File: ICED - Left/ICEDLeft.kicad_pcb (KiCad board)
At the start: 2 copper layers, 175.4 x 145 mm, 148 parts, among them P1 FLASH_HDR, P2 USBC, P3 CONN_17, P4 USB3_AFEMALE, Q1 TC1264, U1 MK20DX256VLH7, X1 CRYSTAL

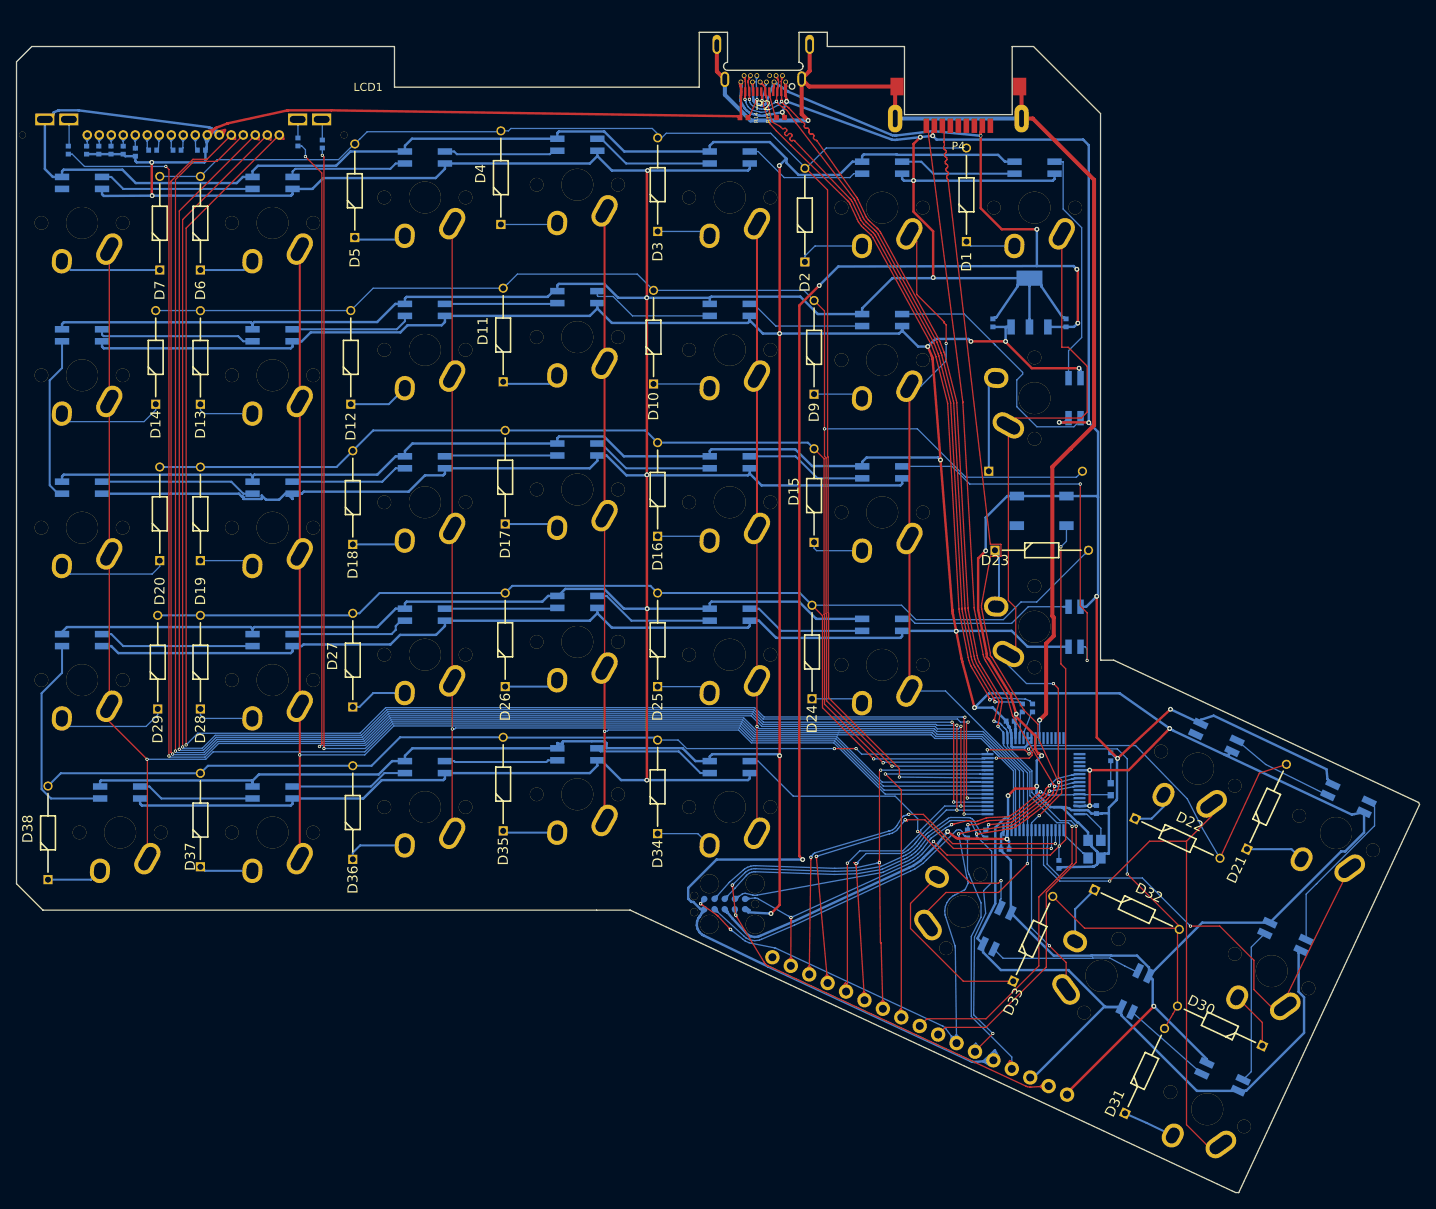
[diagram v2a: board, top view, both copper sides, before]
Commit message: RGB headers and finishing touches!
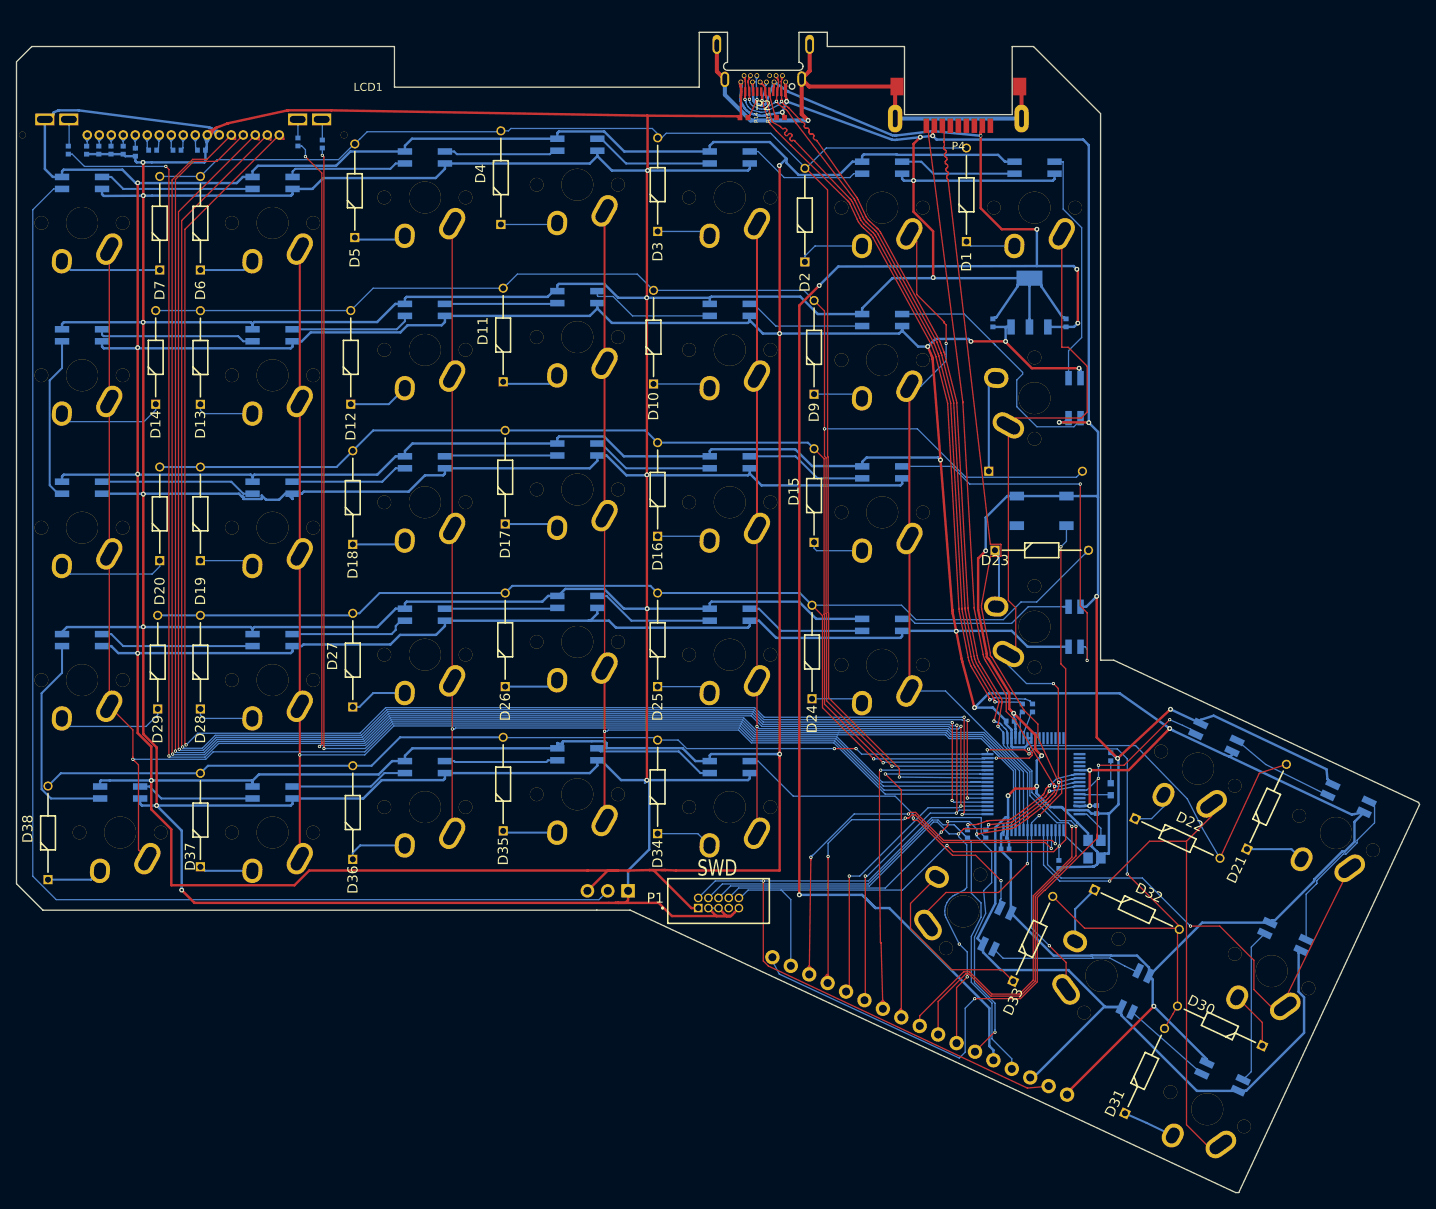
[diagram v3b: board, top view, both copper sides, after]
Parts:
- added P5: RGB Out, Connector_PinHeader_2.54mm:PinHeader_1x03_P2.54mm_Horizontal, B.Cu at (94.1, 133.1)
- P1: value FLASH_HDR -> Conn_ARM_JTAG_SWD_10; footprint prettylib:JLINK_NEEDLE -> prettylib:SHF-105-01-L-D-TH; moved to F.Cu
- moved P1 0.77 mm to (105.4, 134.6), turned to 0 degrees
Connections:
- LED22 pad 4: (no net) -> /ledmatrix/RGBIN
- LED7 pad 2: (no net) -> /ledmatrix/RGBOUT
- P1 pad 5: +5V -> VSS
- P1 pad 7: /mcu/TX2 -> (no net)
- P1 pad 9: /mcu/PTA5 -> VSS
- P3 pad 17: (no net) -> /ledmatrix/RGBIN
- U1 pad 10: /GND -> (no net)
- U1 pad 26: (no net) -> /ledmatrix/RGBIN
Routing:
- net VDD: track 974.2 -> 1142.2 mm, vias 15 -> 19
- net /ledmatrix/RGBOUT: track 0.00 -> 162.0 mm
- net VSS: track 1170.4 -> 1320.3 mm, vias 25 -> 28
- net /ledmatrix/RGBIN: track 0.00 -> 92.8 mm, vias 0 -> 4
- net /GND: track 149.8 -> 64.7 mm, vias 2 -> 1
- net /mcu/PTA5: track 54.0 -> 3.91 mm, vias 2 -> 0
- net +5V: track 248.6 -> 222.8 mm
- net /mcu/TX2: track 70.2 -> 45.2 mm, vias 2 -> 1
- net /mcu/TX0: track 177.4 -> 169.7 mm
- net /mcu/RX1: track 155.3 -> 160.3 mm
- net /mcu/SCLK: track 232.7 -> 227.8 mm
- net /mcu/TX1: track 158.4 -> 162.0 mm
- net /mcu/MOSI: track 232.5 -> 229.6 mm
- net /mcu/RX0: track 177.1 -> 174.4 mm, vias 3 -> 5
- net /Col9: track 189.3 -> 191.1 mm
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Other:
- board text added: "Based on Ergodox Infinity v1.2b"
- board text added: "Ergodox Aleph 1 by @stillinbeta"
- board text added: "RGB Out"
- board text added: "RGBIN"
- board text added: "SWD"
- board text removed: "AUD"
- board text removed: "Ergodox Aleph v0.1 by @stillinbeta"

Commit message: Footprints placed
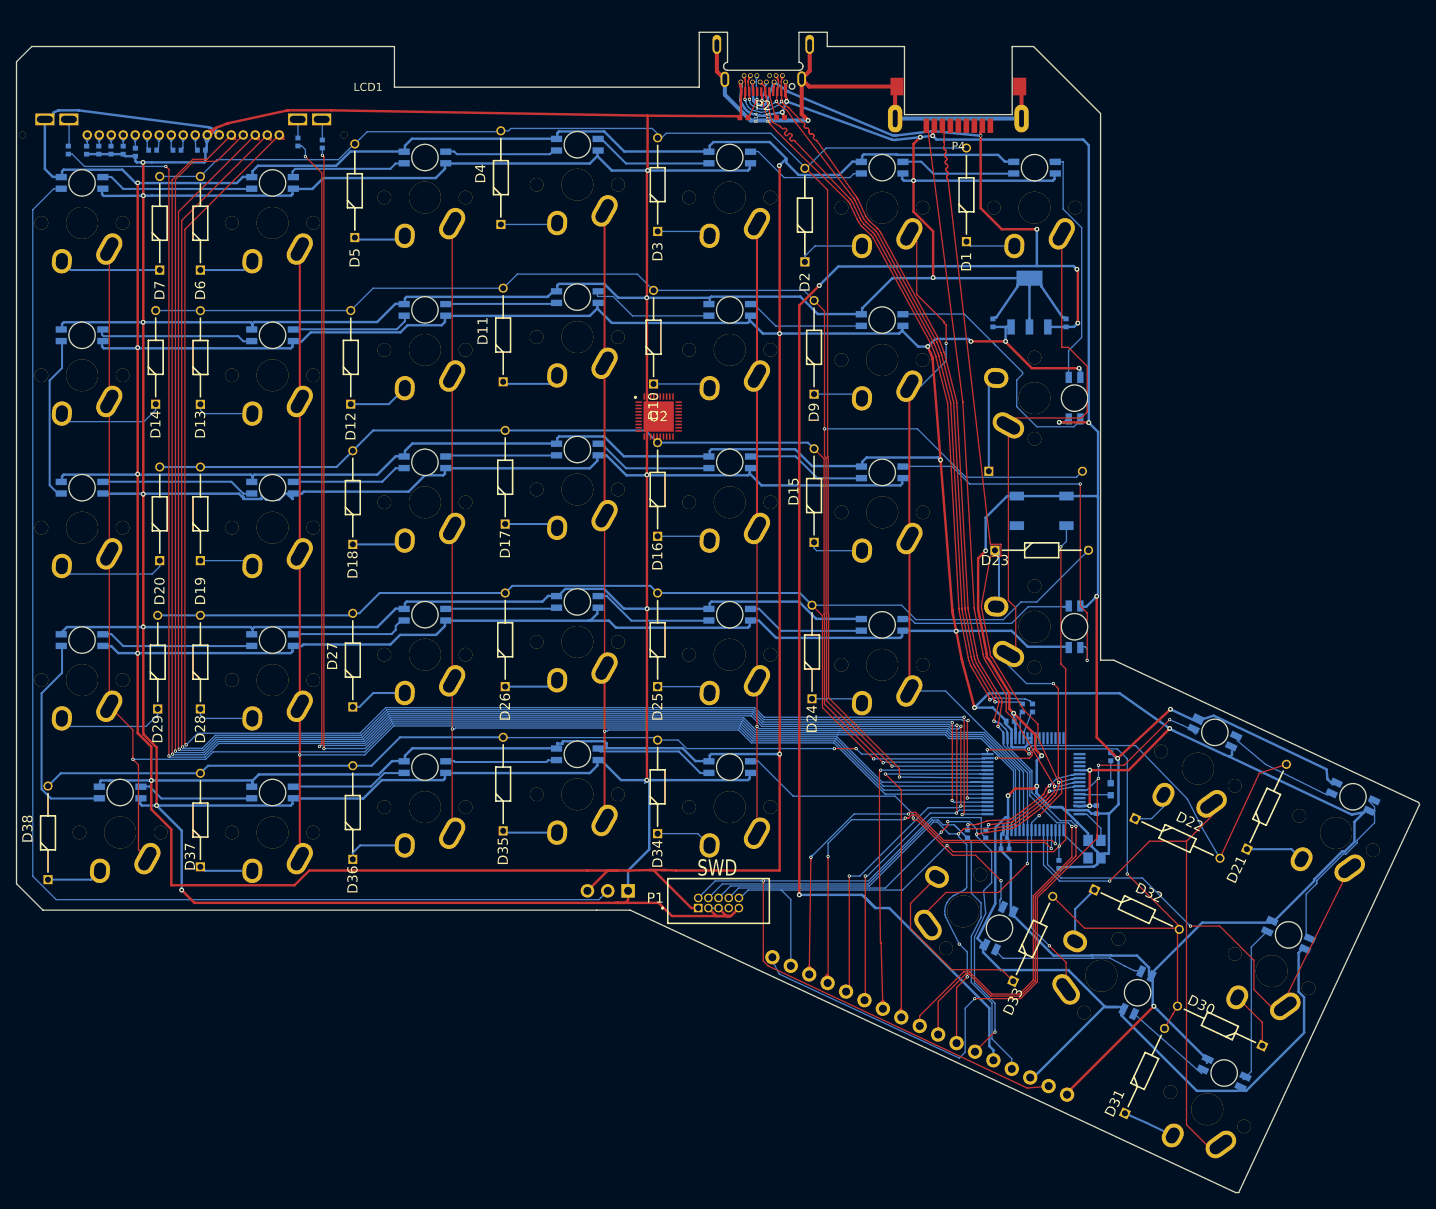
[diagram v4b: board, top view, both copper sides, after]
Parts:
- added U2: IS31FL3737-QFLS4-TR, prettylib:QFN40P500X500X80-41N-D, F.Cu at (97.9, 73.8)
- LED1, LED10, LED11, LED12, LED13, LED14, LED15, LED16, LED17, LED18, LED19, LED2, LED20, LED21, LED22, LED23, LED24, LED25, LED26, LED27, LED28, LED29, LED3, LED30, LED31, LED32, LED33, LED34, LED35, LED36, LED37, LED38, LED4, LED5, LED6, LED7, LED8, LED9: value SK6812MINI-E -> LED_RGBA; footprint prettylib:SK6812MINIE -> prettylib:AAA3528SURKCGKC09
- moved LED22 0.66 mm to (167.4, 113.3)
- moved LED21 0.60 mm to (184.7, 121.3)
- moved LED31 0.51 mm to (168.6, 155.9)
- moved LED30 0.44 mm to (176.7, 138.6)
- moved LED32 0.35 mm to (157.8, 145.8)
- moved LED33 0.32 mm to (140.5, 137.8)
- turned LED1 to 0 degrees
- turned LED15 to 0 degrees
- turned LED16 to 0 degrees
- turned LED17 to 0 degrees
- turned LED18 to 0 degrees
- turned LED19 to 0 degrees
- turned LED2 to 0 degrees
- turned LED20 to 0 degrees
- turned LED3 to 0 degrees
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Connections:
- LED1 pad 1: VDD -> /mcu/ledmatrix_2/Red3
- LED1 pad 2: Net-(LED1-Pad2) -> /mcu/ledmatrix_2/Green3
- LED1 pad 3: VSS -> /mcu/ledmatrix_2/Blue3
- LED1 pad 4: Net-(LED1-Pad4) -> /mcu/ledmatrix_2/Row1B
- LED10 pad 1: VDD -> /mcu/ledmatrix_2/Red1
- LED10 pad 2: Net-(LED10-Pad2) -> /mcu/ledmatrix_2/Green1
- LED10 pad 3: VSS -> /mcu/ledmatrix_2/Blue1
- LED10 pad 4: Net-(LED10-Pad4) -> /mcu/ledmatrix_2/Row2B
- LED11 pad 1: VDD -> /mcu/ledmatrix_2/Red4
- LED11 pad 2: Net-(LED10-Pad4) -> /mcu/ledmatrix_2/Green4
- LED11 pad 3: VSS -> /mcu/ledmatrix_2/Blue4
- LED11 pad 4: Net-(LED11-Pad4) -> /mcu/ledmatrix_2/Row2A
- LED12 pad 1: VDD -> /mcu/ledmatrix_2/Red3
- LED12 pad 2: Net-(LED11-Pad4) -> /mcu/ledmatrix_2/Green3
- LED12 pad 3: VSS -> /mcu/ledmatrix_2/Blue3
- LED12 pad 4: Net-(LED12-Pad4) -> /mcu/ledmatrix_2/Row2A
- LED13 pad 1: VDD -> /mcu/ledmatrix_2/Red2
- LED13 pad 2: Net-(LED12-Pad4) -> /mcu/ledmatrix_2/Green2
- LED13 pad 3: VSS -> /mcu/ledmatrix_2/Blue2
- LED13 pad 4: Net-(LED13-Pad4) -> /mcu/ledmatrix_2/Row2A
- LED14 pad 1: VDD -> /mcu/ledmatrix_2/Red1
- LED14 pad 2: Net-(LED13-Pad4) -> /mcu/ledmatrix_2/Green1
- LED14 pad 3: VSS -> /mcu/ledmatrix_2/Blue1
- LED14 pad 4: Net-(LED14-Pad4) -> /mcu/ledmatrix_2/Row2A
- LED15 pad 1: VDD -> /mcu/ledmatrix_2/Red2
- LED15 pad 2: Net-(LED15-Pad2) -> /mcu/ledmatrix_2/Green2
- LED15 pad 3: VSS -> /mcu/ledmatrix_2/Blue2
- LED15 pad 4: Net-(LED15-Pad4) -> /mcu/ledmatrix_2/Row3B
- LED16 pad 1: VDD -> /mcu/ledmatrix_2/Red1
- LED16 pad 2: Net-(LED16-Pad2) -> /mcu/ledmatrix_2/Green1
- LED16 pad 3: VSS -> /mcu/ledmatrix_2/Blue1
- LED16 pad 4: Net-(LED15-Pad2) -> /mcu/ledmatrix_2/Row3B
- LED17 pad 1: VDD -> /mcu/ledmatrix_2/Red4
- LED17 pad 2: Net-(LED17-Pad2) -> /mcu/ledmatrix_2/Green4
- LED17 pad 3: VSS -> /mcu/ledmatrix_2/Blue4
- LED17 pad 4: Net-(LED16-Pad2) -> /mcu/ledmatrix_2/Row3A
- LED18 pad 1: VDD -> /mcu/ledmatrix_2/Red3
- LED18 pad 2: Net-(LED18-Pad2) -> /mcu/ledmatrix_2/Green3
- LED18 pad 3: VSS -> /mcu/ledmatrix_2/Blue3
- LED18 pad 4: Net-(LED17-Pad2) -> /mcu/ledmatrix_2/Row3A
- LED19 pad 1: VDD -> /mcu/ledmatrix_2/Red2
- LED19 pad 2: Net-(LED19-Pad2) -> /mcu/ledmatrix_2/Green2
- LED19 pad 3: VSS -> /mcu/ledmatrix_2/Blue2
- LED19 pad 4: Net-(LED18-Pad2) -> /mcu/ledmatrix_2/Row3A
- LED2 pad 1: VDD -> /mcu/ledmatrix_2/Red2
- LED2 pad 2: Net-(LED2-Pad2) -> /mcu/ledmatrix_2/Green2
- LED2 pad 3: VSS -> /mcu/ledmatrix_2/Blue2
- LED2 pad 4: Net-(LED1-Pad2) -> /mcu/ledmatrix_2/Row1B
- LED20 pad 1: VDD -> /mcu/ledmatrix_2/Red1
- LED20 pad 2: Net-(LED14-Pad4) -> /mcu/ledmatrix_2/Green1
- LED20 pad 3: VSS -> /mcu/ledmatrix_2/Blue1
- LED20 pad 4: Net-(LED19-Pad2) -> /mcu/ledmatrix_2/Row3A
- LED21 pad 1: VDD -> /mcu/ledmatrix_2/Red2
- LED21 pad 2: Net-(LED21-Pad2) -> /mcu/ledmatrix_2/Green2
- LED21 pad 3: VSS -> /mcu/ledmatrix_2/Blue2
- LED21 pad 4: Net-(LED21-Pad4) -> /mcu/ledmatrix_2/Row4C
- LED22 pad 1: VDD -> /mcu/ledmatrix_2/Red1
- LED22 pad 2: Net-(LED21-Pad4) -> /mcu/ledmatrix_2/Green1
- LED22 pad 3: VSS -> /mcu/ledmatrix_2/Blue1
- LED22 pad 4: /ledmatrix/RGBIN -> /mcu/ledmatrix_2/Row4C
- LED23 pad 1: VDD -> /mcu/ledmatrix_2/Red3
- LED23 pad 2: Net-(LED15-Pad4) -> /mcu/ledmatrix_2/Green3
- LED23 pad 3: VSS -> /mcu/ledmatrix_2/Blue3
- LED23 pad 4: Net-(LED23-Pad4) -> /mcu/ledmatrix_2/Row4B
- LED24 pad 1: VDD -> /mcu/ledmatrix_2/Red2
- LED24 pad 2: Net-(LED23-Pad4) -> /mcu/ledmatrix_2/Green2
- LED24 pad 3: VSS -> /mcu/ledmatrix_2/Blue2
- LED24 pad 4: Net-(LED24-Pad4) -> /mcu/ledmatrix_2/Row4B
- LED25 pad 1: VDD -> /mcu/ledmatrix_2/Red1
- LED25 pad 2: Net-(LED24-Pad4) -> /mcu/ledmatrix_2/Green1
- LED25 pad 3: VSS -> /mcu/ledmatrix_2/Blue1
- LED25 pad 4: Net-(LED25-Pad4) -> /mcu/ledmatrix_2/Row4B
- LED26 pad 1: VDD -> /mcu/ledmatrix_2/Red4
- LED26 pad 2: Net-(LED25-Pad4) -> /mcu/ledmatrix_2/Green4
- LED26 pad 3: VSS -> /mcu/ledmatrix_2/Blue4
- LED26 pad 4: Net-(LED26-Pad4) -> /mcu/ledmatrix_2/Row4A
- LED27 pad 1: VDD -> /mcu/ledmatrix_2/Red3
- LED27 pad 2: Net-(LED26-Pad4) -> /mcu/ledmatrix_2/Green3
- LED27 pad 3: VSS -> /mcu/ledmatrix_2/Blue3
- LED27 pad 4: Net-(LED27-Pad4) -> /mcu/ledmatrix_2/Row4A
- LED28 pad 1: VDD -> /mcu/ledmatrix_2/Red2
- LED28 pad 2: Net-(LED27-Pad4) -> /mcu/ledmatrix_2/Green2
- LED28 pad 3: VSS -> /mcu/ledmatrix_2/Blue2
- LED28 pad 4: Net-(LED28-Pad4) -> /mcu/ledmatrix_2/Row4A
- LED29 pad 1: VDD -> /mcu/ledmatrix_2/Red1
- LED29 pad 2: Net-(LED28-Pad4) -> /mcu/ledmatrix_2/Green1
- LED29 pad 3: VSS -> /mcu/ledmatrix_2/Blue1
- LED29 pad 4: Net-(LED29-Pad4) -> /mcu/ledmatrix_2/Row4A
- LED3 pad 1: VDD -> /mcu/ledmatrix_2/Red1
- LED3 pad 2: Net-(LED3-Pad2) -> /mcu/ledmatrix_2/Green1
- LED3 pad 3: VSS -> /mcu/ledmatrix_2/Blue1
- LED3 pad 4: Net-(LED2-Pad2) -> /mcu/ledmatrix_2/Row1B
- LED30 pad 1: VDD -> /mcu/ledmatrix_2/Red3
- LED30 pad 2: Net-(LED30-Pad2) -> /mcu/ledmatrix_2/Green3
- LED30 pad 3: VSS -> /mcu/ledmatrix_2/Blue3
- LED30 pad 4: Net-(LED21-Pad2) -> /mcu/ledmatrix_2/Row4C
- LED31 pad 1: VDD -> /mcu/ledmatrix_2/Red4
- LED31 pad 2: Net-(LED31-Pad2) -> /mcu/ledmatrix_2/Green4
- LED31 pad 3: VSS -> /mcu/ledmatrix_2/Blue4
- LED31 pad 4: Net-(LED30-Pad2) -> /mcu/ledmatrix_2/Row5B
- LED32 pad 1: VDD -> /mcu/ledmatrix_2/Red3
- LED32 pad 2: Net-(LED32-Pad2) -> /mcu/ledmatrix_2/Green3
- LED32 pad 3: VSS -> /mcu/ledmatrix_2/Blue3
- LED32 pad 4: Net-(LED31-Pad2) -> /mcu/ledmatrix_2/Row5B
- LED33 pad 1: VDD -> /mcu/ledmatrix_2/Red2
- LED33 pad 2: Net-(LED33-Pad2) -> /mcu/ledmatrix_2/Green2
- LED33 pad 3: VSS -> /mcu/ledmatrix_2/Blue2
- LED33 pad 4: Net-(LED32-Pad2) -> /mcu/ledmatrix_2/Row5B
- LED34 pad 1: VDD -> /mcu/ledmatrix_2/Red1
- LED34 pad 2: Net-(LED34-Pad2) -> /mcu/ledmatrix_2/Green1
- LED34 pad 3: VSS -> /mcu/ledmatrix_2/Blue1
- LED34 pad 4: Net-(LED33-Pad2) -> /mcu/ledmatrix_2/Row5B
- LED35 pad 1: VDD -> /mcu/ledmatrix_2/Red4
- LED35 pad 2: Net-(LED35-Pad2) -> /mcu/ledmatrix_2/Green4
- LED35 pad 3: VSS -> /mcu/ledmatrix_2/Blue4
- LED35 pad 4: Net-(LED34-Pad2) -> /mcu/ledmatrix_2/Row5A
- LED36 pad 1: VDD -> /mcu/ledmatrix_2/Red3
- LED36 pad 2: Net-(LED36-Pad2) -> /mcu/ledmatrix_2/Green3
- LED36 pad 3: VSS -> /mcu/ledmatrix_2/Blue3
- LED36 pad 4: Net-(LED35-Pad2) -> /mcu/ledmatrix_2/Row5A
- LED37 pad 1: VDD -> /mcu/ledmatrix_2/Red2
- LED37 pad 2: Net-(LED37-Pad2) -> /mcu/ledmatrix_2/Green2
- LED37 pad 3: VSS -> /mcu/ledmatrix_2/Blue2
- LED37 pad 4: Net-(LED36-Pad2) -> /mcu/ledmatrix_2/Row5A
- LED38 pad 1: VDD -> /mcu/ledmatrix_2/Red1
- LED38 pad 2: Net-(LED29-Pad4) -> /mcu/ledmatrix_2/Green1
- LED38 pad 3: VSS -> /mcu/ledmatrix_2/Blue1
- LED38 pad 4: Net-(LED37-Pad2) -> /mcu/ledmatrix_2/Row5A
- LED4 pad 1: VDD -> /mcu/ledmatrix_2/Red4
- LED4 pad 2: Net-(LED4-Pad2) -> /mcu/ledmatrix_2/Green4
- LED4 pad 3: VSS -> /mcu/ledmatrix_2/Blue4
- LED4 pad 4: Net-(LED3-Pad2) -> /mcu/ledmatrix_2/Row1A
- LED5 pad 1: VDD -> /mcu/ledmatrix_2/Red3
- LED5 pad 2: Net-(LED5-Pad2) -> /mcu/ledmatrix_2/Green3
- LED5 pad 3: VSS -> /mcu/ledmatrix_2/Blue3
- LED5 pad 4: Net-(LED4-Pad2) -> /mcu/ledmatrix_2/Row1A
- LED6 pad 1: VDD -> /mcu/ledmatrix_2/Red2
- LED6 pad 2: Net-(LED6-Pad2) -> /mcu/ledmatrix_2/Green2
- LED6 pad 3: VSS -> /mcu/ledmatrix_2/Blue2
- LED6 pad 4: Net-(LED5-Pad2) -> /mcu/ledmatrix_2/Row1A
- LED7 pad 1: VDD -> /mcu/ledmatrix_2/Red1
- LED7 pad 2: /ledmatrix/RGBOUT -> /mcu/ledmatrix_2/Green1
- LED7 pad 3: VSS -> /mcu/ledmatrix_2/Blue1
- LED7 pad 4: Net-(LED6-Pad2) -> /mcu/ledmatrix_2/Row1A
- LED8 pad 1: VDD -> /mcu/ledmatrix_2/Red3
- LED8 pad 2: Net-(LED1-Pad4) -> /mcu/ledmatrix_2/Green3
- LED8 pad 3: VSS -> /mcu/ledmatrix_2/Blue3
- LED8 pad 4: Net-(LED8-Pad4) -> /mcu/ledmatrix_2/Row2B
- LED9 pad 1: VDD -> /mcu/ledmatrix_2/Red2
- LED9 pad 2: Net-(LED8-Pad4) -> /mcu/ledmatrix_2/Green2
- LED9 pad 3: VSS -> /mcu/ledmatrix_2/Blue2
- LED9 pad 4: Net-(LED10-Pad2) -> /mcu/ledmatrix_2/Row2B
- P3 pad 17: /ledmatrix/RGBIN -> /mcu/RGBIN
- P5 pad 2: /ledmatrix/RGBOUT -> (no net)
- U1 pad 26: /ledmatrix/RGBIN -> /mcu/RGBIN
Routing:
- net (no net): track 0.00 -> 177.2 mm
- net /ledmatrix/RGBOUT: track 162.0 -> 0.00 mm
- net /mcu/ledmatrix_2/Green3: track 0.00 -> 66.0 mm
- net /mcu/ledmatrix_2/Row1A: track 0.00 -> 49.1 mm
- net /mcu/ledmatrix_2/Row3A: track 0.00 -> 48.9 mm
- net Net-(LED15-Pad4): track 48.1 -> 0.00 mm, vias 2 -> 0
- net /mcu/ledmatrix_2/Row4B: track 0.00 -> 48.1 mm, vias 0 -> 2
- net /mcu/ledmatrix_2/Green1: track 0.00 -> 47.4 mm
- net /mcu/ledmatrix_2/Row5A: track 0.00 -> 44.2 mm
- net Net-(LED33-Pad2): track 41.5 -> 0.00 mm, vias 2 -> 0
- net /mcu/ledmatrix_2/Row5B: track 0.00 -> 41.5 mm, vias 0 -> 2
- net /mcu/ledmatrix_2/Row1B: track 0.00 -> 30.3 mm
- net Net-(LED1-Pad4): track 30.1 -> 0.37 mm
- net /mcu/ledmatrix_2/Row2B: track 0.00 -> 29.8 mm
- net Net-(LED29-Pad4): track 26.7 -> 0.00 mm
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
